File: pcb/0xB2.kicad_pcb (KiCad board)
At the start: 2 copper layers, 17.8 x 33 mm, 42 parts, among them J1 USB_C_Receptacle_USB2.0, J2 Conn_01x12, J3 Conn_01x05, J4 Conn_01x12, J5 Conn_01x02, SW1 SW_Push, SW2 SW_Push, U1 RP2040, U2 W25Q32JVZP, U3 XC6210B332MR-G, Y1 Crystal_GND24

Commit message: Get v2 ready for manufacturing
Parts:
- U2: value W25Q32JVZP -> GD25Q80CEIGR
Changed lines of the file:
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@@
     (property "Sheetfile" "0xB2.kicad_sch")
     (property "Sheetname" "")
+    (property "exclude_from_bom" "")
     (attr through_hole exclude_from_pos_files exclude_from_bom)
     (fp_text reference "J3" (at 0 -1.905 90) (layer "F.SilkS") hide
@@
     (property "Sheetfile" "0xB2.kicad_sch")
     (property "Sheetname" "")
+    (property "exclude_from_bom" "")
     (attr through_hole exclude_from_pos_files exclude_from_bom)
     (fp_text reference "J2" (at 0 -1.905 180) (layer "F.SilkS") hide
@@
       (effects (font (size 0.8 0.8) (thickness 0.15)))
     )
-    (fp_text value "W25Q32JVZP" (at 0 2.1) (layer "F.Fab")
+    (fp_text value "GD25Q80CEIGR" (at 0 2.1) (layer "F.Fab")
       (effects (font (size 1 1) (thickness 0.15)))
     )
@@
     (property "Sheetfile" "0xB2.kicad_sch")
     (property "Sheetname" "")
+    (property "exclude_from_bom" "")
     (attr through_hole exclude_from_pos_files exclude_from_bom)
     (fp_text reference "J4" (at 0 -1.905) (layer "F.SilkS") hide
@@
     (property "Sheetfile" "0xB2.kicad_sch")
     (property "Sheetname" "")
+    (property "exclude_from_bom" "")
     (attr through_hole exclude_from_pos_files exclude_from_bom)
     (fp_text reference "J5" (at 0 -1.695) (layer "F.SilkS") hide

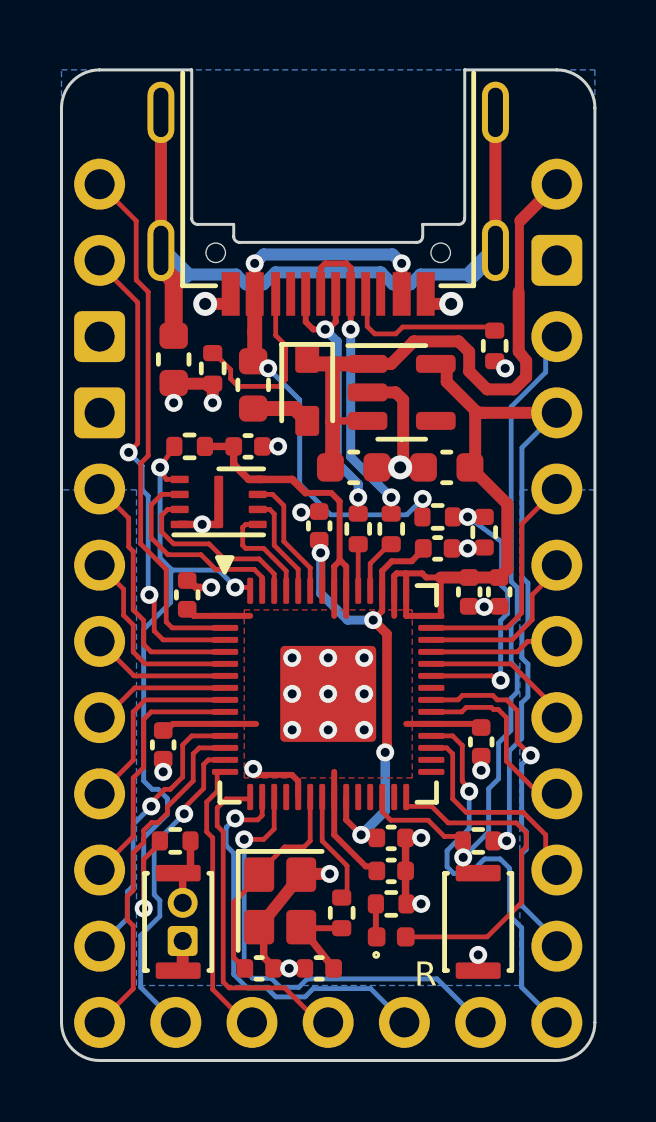
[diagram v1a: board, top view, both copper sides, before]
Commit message: Update pinout
Use of the agreed pinout (see discussions on bkb discord)
for bottom row and VBUS detect.
Maintain compatibility with Sparkfun RP2040.
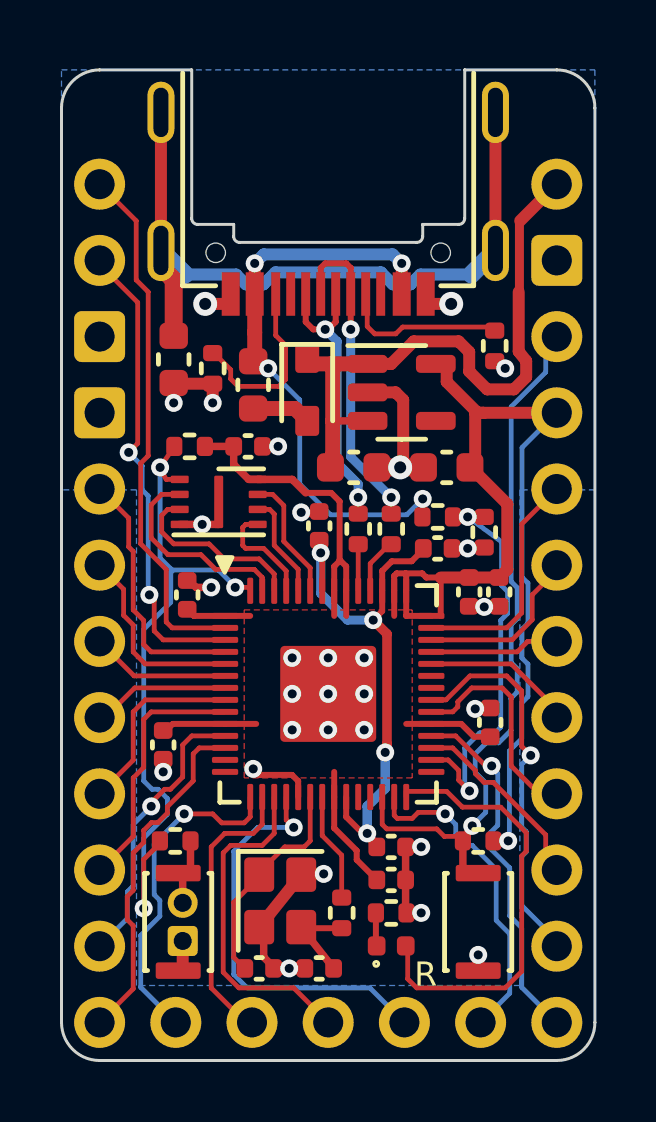
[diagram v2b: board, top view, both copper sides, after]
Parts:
- removed rb_cake: G*****, 0xB2_drawings:rb_cake
- removed splinky: G*****, 0xB2_drawings:splinky
- moved C13 0.72 mm to (157.8, 98.0), turned to 90 degrees
- moved D1 0.30 mm to (154.5, 105.4)
- moved C14 0.30 mm to (154.5, 103.2)
- moved C8 0.30 mm to (154.5, 102.1)
- moved R1 0.30 mm to (154.5, 104.3)
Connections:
- J3 pad 1: /D10 -> /D12
- J3 pad 2: /D11 -> /D13
- J3 pad 3: /D12 -> /D14
- J3 pad 4: /D13 -> /D15
- J3 pad 5: /D14 -> /D16
- U1 pad 13: /D10 -> unconnected-(U1-Pad13)
- U1 pad 14: /D11 -> unconnected-(U1-Pad14)
- U1 pad 18: unconnected-(U1-Pad18) -> /D15
- U1 pad 27: unconnected-(U1-Pad27) -> /D16
- U1 pad 30: unconnected-(U1-Pad30) -> /VBUS_DET
- U1 pad 37: /VBUS_DET -> unconnected-(U1-Pad37)
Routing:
- net /D15: track 0.00 -> 13.9 mm, vias 0 -> 1
- net /D10: track 10.9 -> 0.00 mm, vias 1 -> 0
- net /D16: track 0.00 -> 10.8 mm, vias 0 -> 1
- net /D11: track 9.51 -> 0.00 mm
- net /D13: track 13.6 -> 9.46 mm, vias 1 -> 0
- net /VBUS_DET: track 9.59 -> 13.7 mm
- net /D14: track 15.4 -> 11.4 mm, vias 1 -> 0
- net /LED: track 11.4 -> 14.7 mm
- net /D21: track 13.9 -> 12.1 mm
- net /SCLK: track 6.29 -> 7.42 mm
- net /MOSI: track 11.9 -> 12.9 mm
- net /MISO: track 7.22 -> 6.40 mm
- net +3V3: track 59.4 -> 60.0 mm
- net /D12: track 11.2 -> 11.3 mm, vias 0 -> 1

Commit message: Silkscreen correction
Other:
- board text added: "v3"
- board text removed: "v2"
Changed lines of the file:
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@@
       (effects (font (size 1 1) (thickness 0.15)))
     )
-    (fp_text user "D10" (at 1.35 0.03 unlocked) (layer "B.SilkS")
+    (fp_text user "D12" (at 1.35 0.03 unlocked) (layer "B.SilkS")
       (effects (font (size 0.6 0.6) (thickness 0.15)) (justify mirror))
     )
-    (fp_text user "D12" (at 1.375 5.055 unlocked) (layer "B.SilkS")
+    (fp_text user "D14" (at 1.375 5.055 unlocked) (layer "B.SilkS")
       (effects (font (size 0.6 0.6) (thickness 0.15)) (justify mirror))
     )
-    (fp_text user "D11" (at 1.375 2.53 unlocked) (layer "B.SilkS")
+    (fp_text user "D13" (at 1.375 2.53 unlocked) (layer "B.SilkS")
       (effects (font (size 0.6 0.6) (thickness 0.15)) (justify mirror))
     )
-    (fp_text user "D13" (at 1.375 7.605 unlocked) (layer "B.SilkS")
+    (fp_text user "D15" (at 1.375 7.605 unlocked) (layer "B.SilkS")
       (effects (font (size 0.6 0.6) (thickness 0.15)) (justify mirror))
     )
-    (fp_text user "D14" (at 1.375 9.78 unlocked) (layer "B.SilkS")
+    (fp_text user "D16" (at 1.375 9.78 unlocked) (layer "B.SilkS")
       (effects (font (size 0.6 0.6) (thickness 0.15)) (justify mirror))
     )
@@
   (gr_arc (start 143.51 77.47) (mid 143.881974 76.571974) (end 144.78 76.2) (layer "Edge.Cuts") (width 0.1))
   (gr_line (start 149.45 81.95) (end 155.35 81.95) (layer "Edge.Cuts") (width 0.1))
-  (gr_text "v2" (at 148.9 105.35) (layer "B.SilkS")
+  (gr_text "v3" (at 148.9 105.35) (layer "B.SilkS")
     (effects (font (size 0.6 0.6) (thickness 0.15)) (justify mirror))
   )

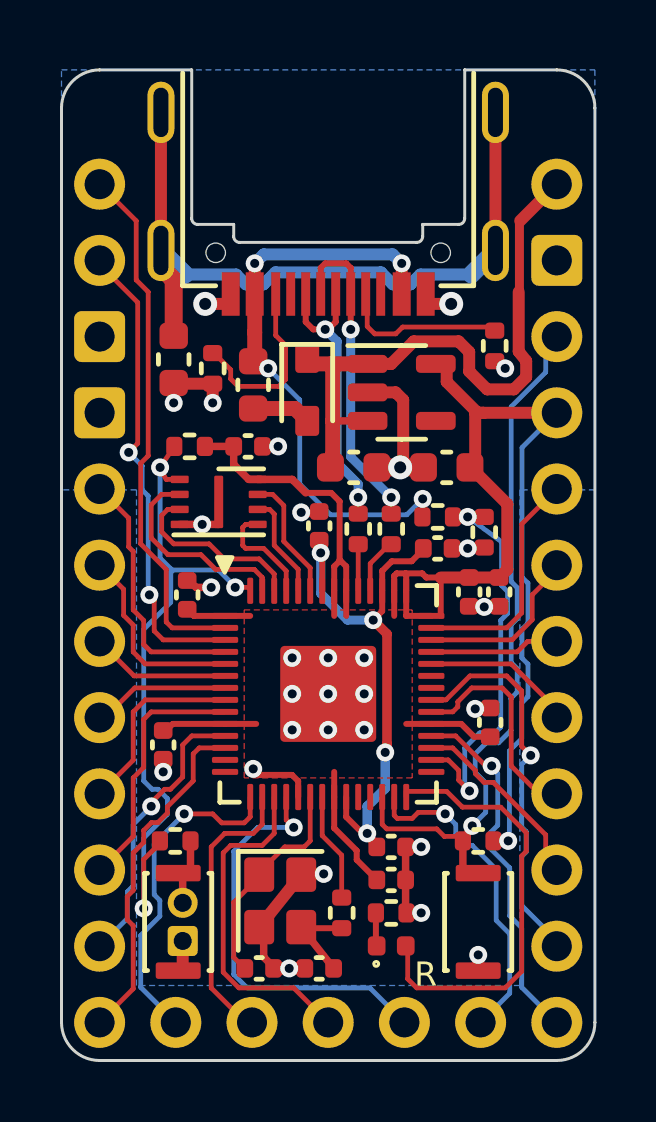
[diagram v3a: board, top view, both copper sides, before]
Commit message: Switch USB-C connector
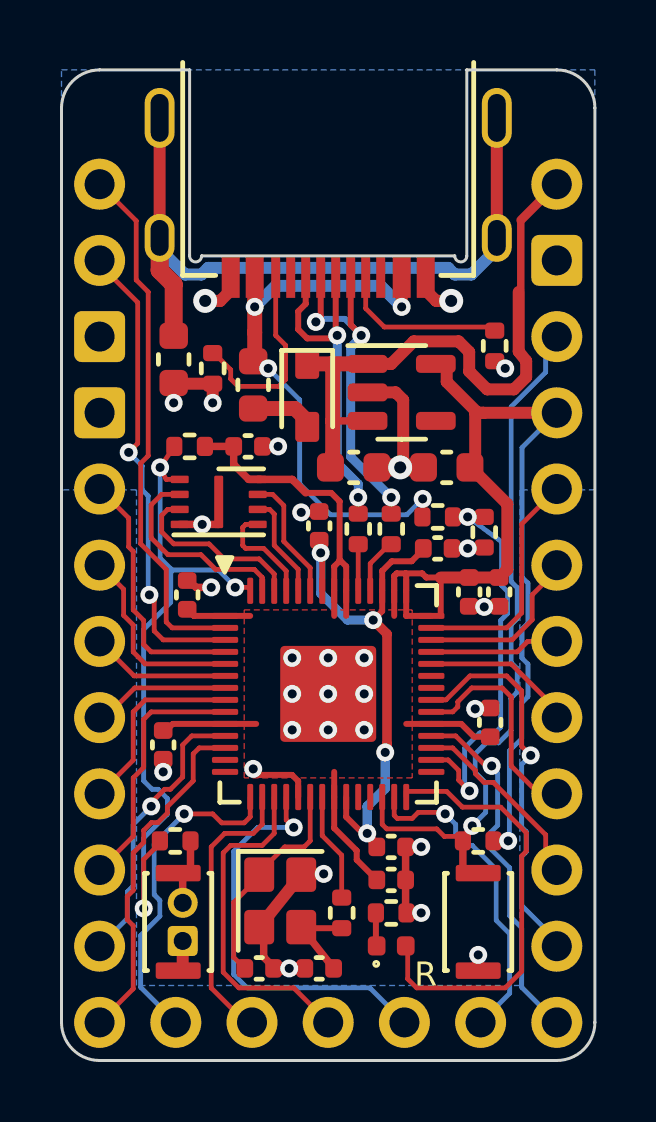
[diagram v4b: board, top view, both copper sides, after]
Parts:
- J1: footprint 0xLib_USB_Type-C:USB_C_Receptacle_HRO_TYPE-C-31-M-14 -> 0xLib_USB_Type-C:USB_C_Receptacle_HRO_TYPE-C-31-M-13B
- moved J1 6.60 mm to (152.4, 75.7)
- moved D2 0.20 mm to (151.7, 87.0)
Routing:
- net /D-: track 10.2 -> 11.5 mm, vias 2 -> 3
- net /D+: track 9.12 -> 10.4 mm
- net Net-(J1-PadB5): track 6.15 -> 6.72 mm
- net GND: track 29.8 -> 30.3 mm
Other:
- outline, holes or cut-outs redrawn

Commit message: Silkscreen correction
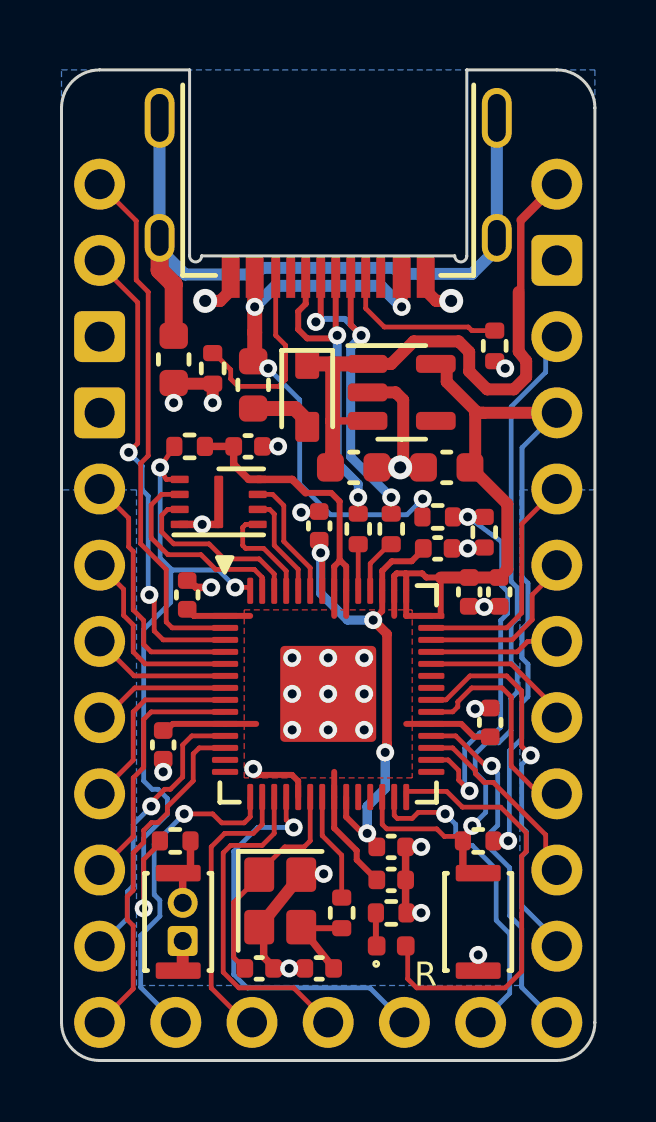
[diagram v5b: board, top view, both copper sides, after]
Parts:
- added REF**: OSHW-Logo_5.7x6mm_SilkScreen, Symbol:OSHW-Logo_5.7x6mm_SilkScreen, B.Cu at (152.8, 87.2)
- added rb_cake: G*****, 0xB2_drawings:rb_cake, B.Cu at (155.9, 91.2)
- added splinky: G*****, 0xB2_drawings:splinky, B.Cu at (156.3, 101.2)
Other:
- board text added: "CERN-OHL-S v2"
- board text added: "v3.1"
- board text removed: "v3"
